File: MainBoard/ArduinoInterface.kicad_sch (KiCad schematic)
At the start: 22 parts, among them J2 SDCard Header, U1 74HC165, U1 IDT7024L15PFG, U10 74HC595, U2 74HC165, U2 ATF22V10C, U4 74HC595, U5 74AHCT04, U7 74HC595, U8 74HC595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

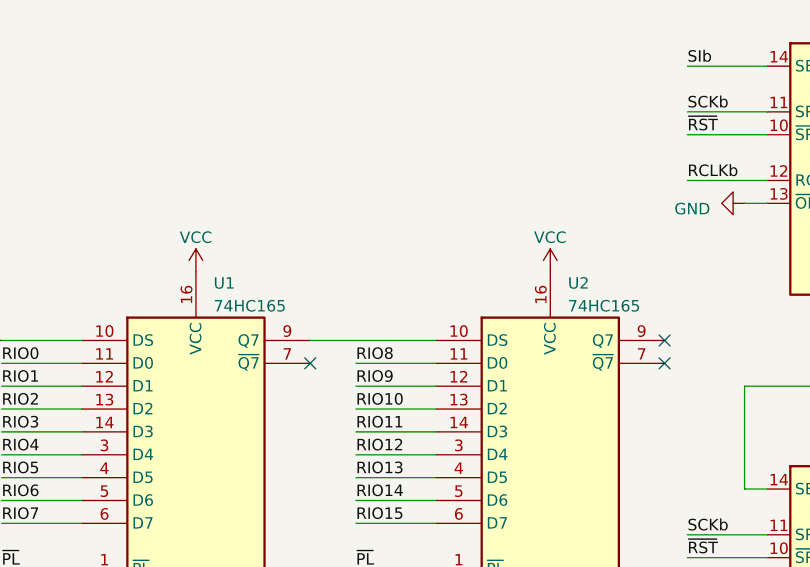
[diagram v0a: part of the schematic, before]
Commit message: MainBoard: Update BOM, PCB printout, and Gerber plots
This includes changes to add the Arduino interface to the main board PCB.
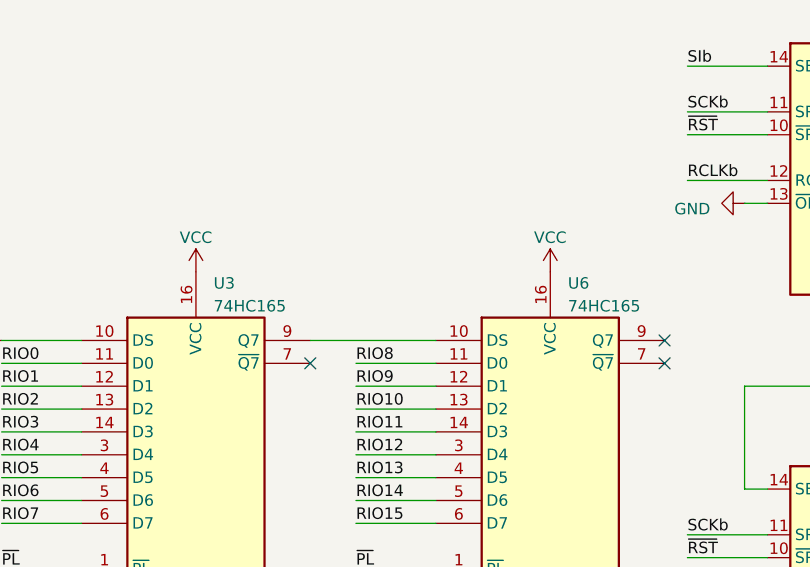
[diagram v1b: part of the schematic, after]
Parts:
- renumbered U1 to U3, U2 to U6
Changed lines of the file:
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@@
   (symbol (lib_id "74xx:74HC165") (at 162.56 71.12 0) (unit 1)
     (in_bom yes) (on_board yes) (dnp no) (fields_autoplaced)
-    (property "Reference" "U2" (at 164.5159 49.53 0)
+    (property "Reference" "U6" (at 164.5159 49.53 0)
       (effects (font (size 1.27 1.27)) (justify left))
     )
@@
   (symbol (lib_id "74xx:74HC165") (at 123.19 71.12 0) (unit 1)
     (in_bom yes) (on_board yes) (dnp no) (fields_autoplaced)
-    (property "Reference" "U1" (at 125.1459 49.53 0)
+    (property "Reference" "U3" (at 125.1459 49.53 0)
       (effects (font (size 1.27 1.27)) (justify left))
     )
@@
   (symbol (lib_id "power:GND") (at 162.56 96.52 0) (unit 1)
     (in_bom yes) (on_board yes) (dnp no) (fields_autoplaced)
-    (property "Reference" "#PWR026" (at 162.56 102.87 0)
+    (property "Reference" "#PWR029" (at 162.56 102.87 0)
       (effects (font (size 1.27 1.27)) hide)
     )
@@
   (symbol (lib_id "power:VCC") (at 162.56 48.26 0) (unit 1)
     (in_bom yes) (on_board yes) (dnp no) (fields_autoplaced)
-    (property "Reference" "#PWR025" (at 162.56 52.07 0)
-      (effects (font (size 1.27 1.27)) hide)
-    )
+    (property "Reference" "#PWR028" (at 162.56 52.07 0)
+      (effects (font (size 1.27 1.27)) hide)
+    )

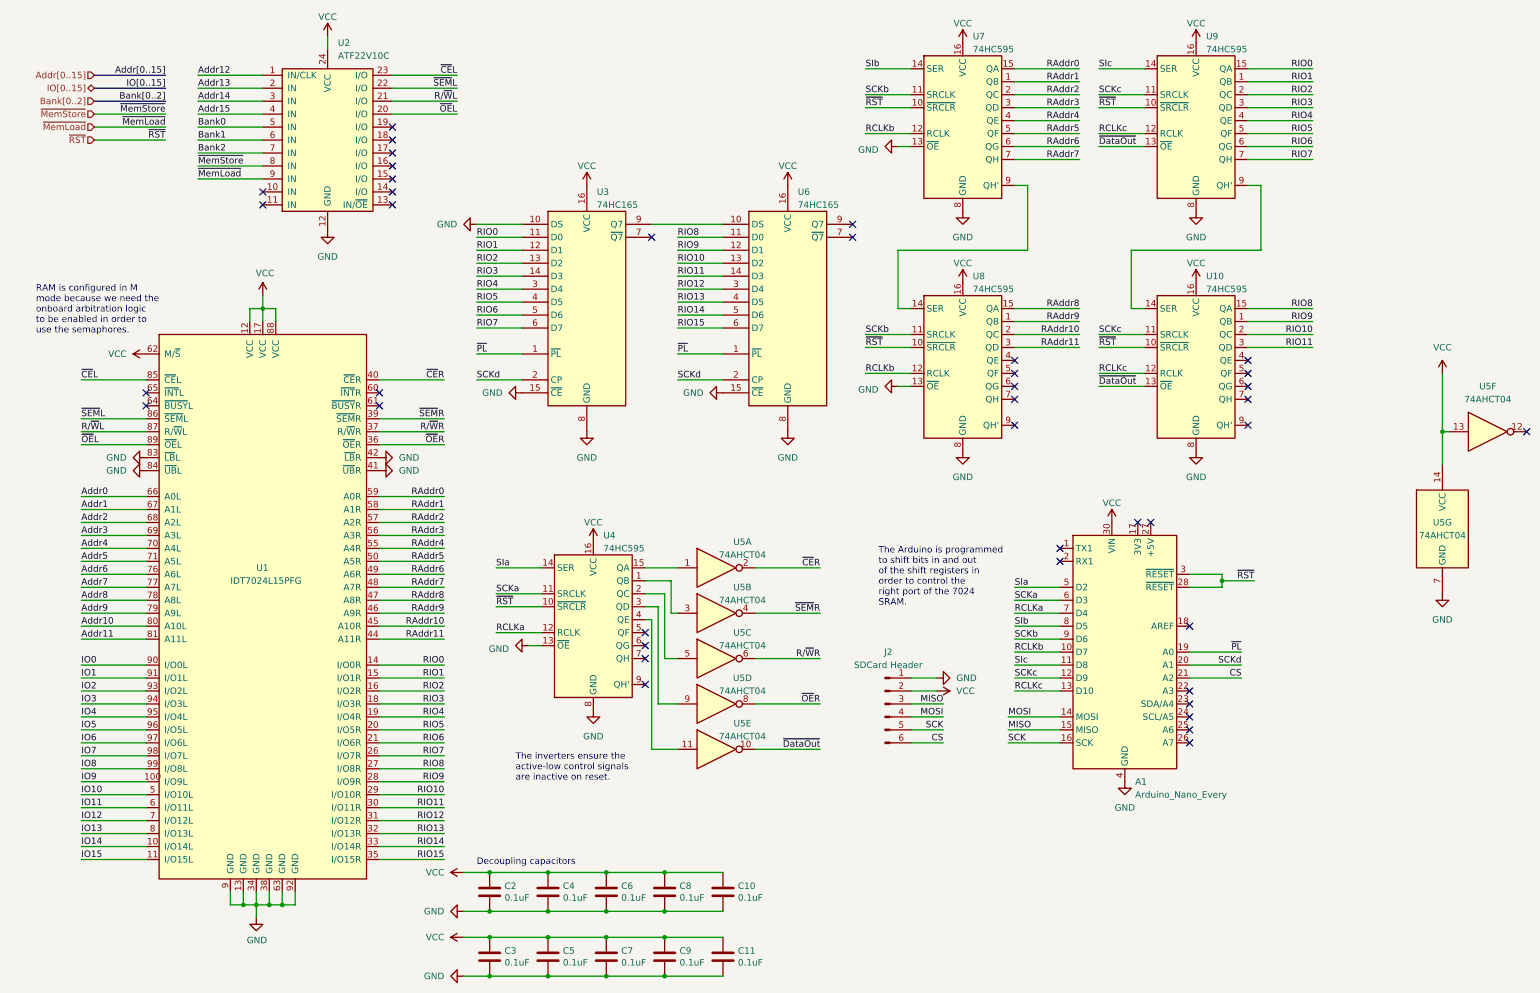
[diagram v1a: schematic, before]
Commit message: MainBoard: Use footprints symbols from the Turtle16 library
These symbols will be consistent across the Turtle16 project and will each
contain manufacturer, mfr. #, Mouser #, and Digikey #.
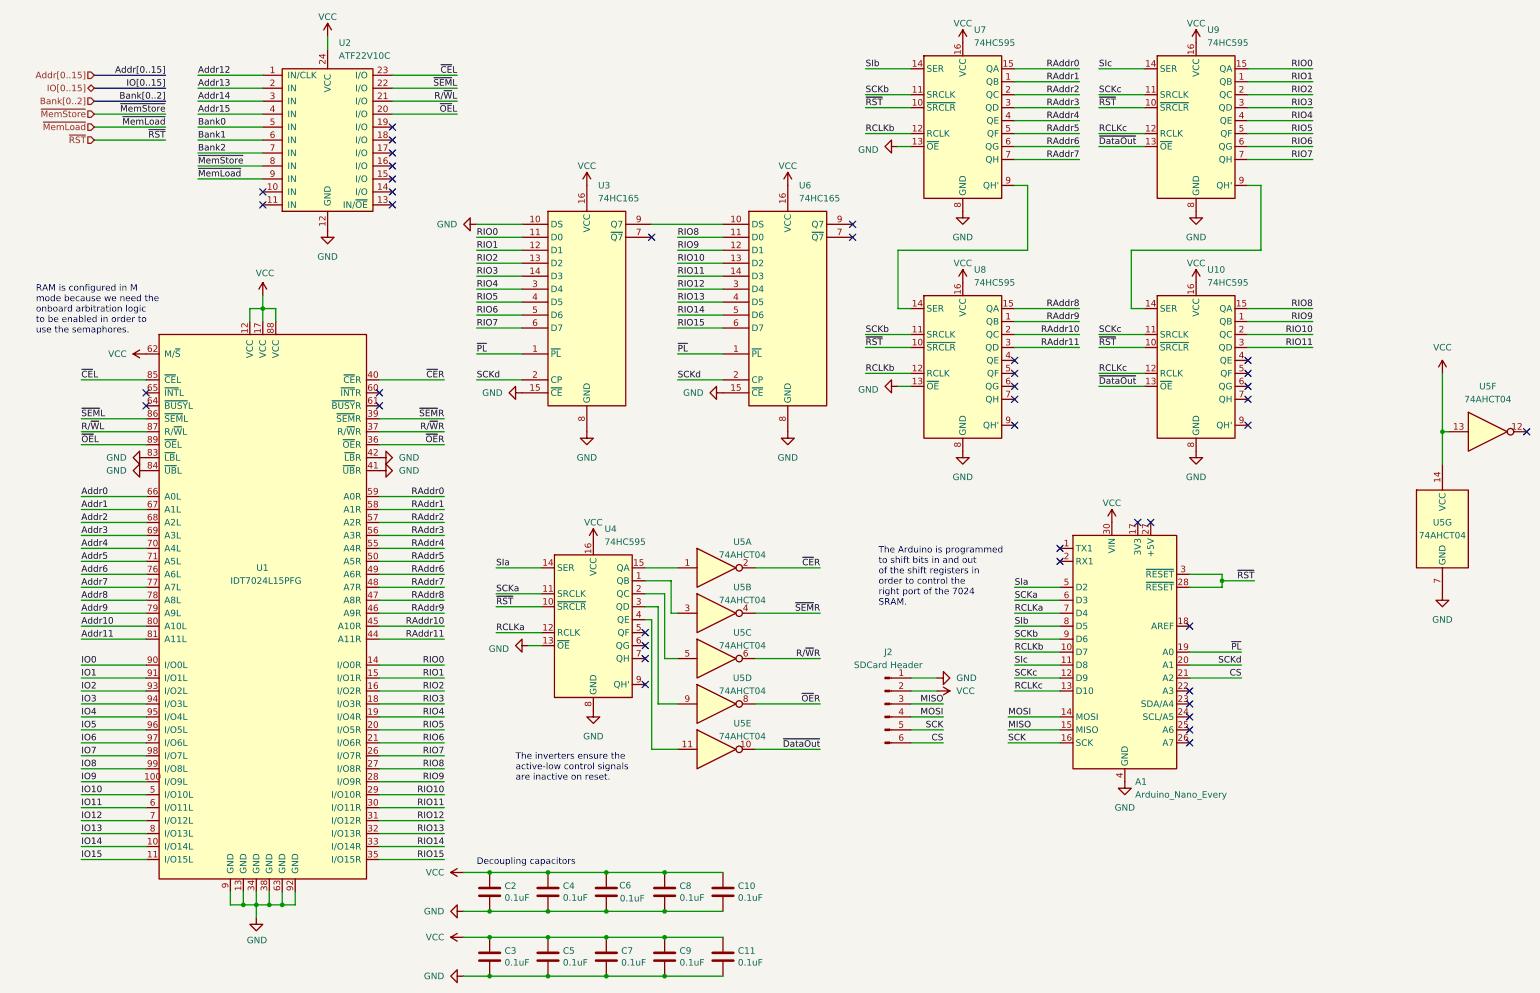
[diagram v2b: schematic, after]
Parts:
- C10, C11, C2, C3, C4, C5, C6, C7, C8, C9: footprint Capacitor_SMD:C_0603_1608Metric_Pad1.08x0.95mm_HandSolder -> Capacitor_SMD:C_0603_1608Metric; Digikey# (none) -> 587-6004-1-ND; Manufacturer (none) -> Taiyo Yuden; Manufacturer# (none) -> EMK107B7104KAHT; Mouser https://www.mouser.com/ProductDetail/963-EMK107B7104KAHT -> (none); Mouser# (none) -> 963-EMK107B7104KAHT
- U1: symbol MainBoard-rescue:IDT7024L15PFG-Memory_RAM -> Turtle16:IDT7024L15PFG; Digikey# (none) -> 800-3611-ND; Manufacturer (none) -> Renesas Electronics Corporation; Manufacturer# (none) -> 7024L15PFG; Mouser https://www.mouser.com/ProductDetail/Renesas-IDT/7024L15PFG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 -> (none); Mouser# (none) -> 972-7024L15PFG
- U10, U4, U7, U8, U9: symbol 74xx:74HC595 -> Turtle16:74HC595; Digikey# (none) -> 1727-1012-1-ND; Manufacturer (none) -> Nexperia; Manufacturer# (none) -> 74HC595PW-Q100,118; Mouser# (none) -> 771-74HC595PW-Q100
- U2: symbol MEMModule-rescue:ATF22V10C-Logic_Programmable -> Turtle16:ATF22V10C; Digikey# (none) -> ATF22V10C-7PX-ND; Manufacturer (none) -> Microchip Technology; Manufacturer# (none) -> ATF22V10C-7PX; Mouser# (none) -> 556-AF22V10C7PX
- U3, U6: symbol 74xx:74HC165 -> Turtle16:74HC165; Digikey# (none) -> 1727-8390-1-ND; Manufacturer (none) -> Nexperia; Manufacturer# (none) -> 74HC165PW-Q100,118; Mouser# (none) -> 771-74HC165PWQ100118
- U5: symbol 74xx:74AHCT04 -> Turtle16:74AHCT04; Digikey# (none) -> 1727-74AHCT04APWJCT-ND; Manufacturer (none) -> Nexperia; Manufacturer# (none) -> 74AHCT04APWJ; Mouser# (none) -> 771-74AHCT04APWJ

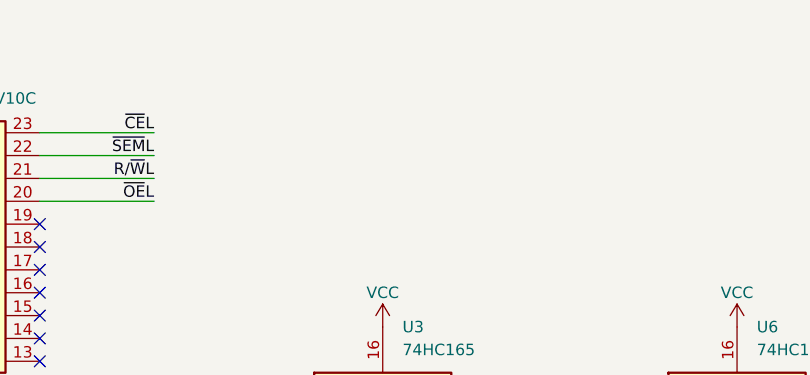
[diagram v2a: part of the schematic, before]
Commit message: MainBoard: Move all components to the top side
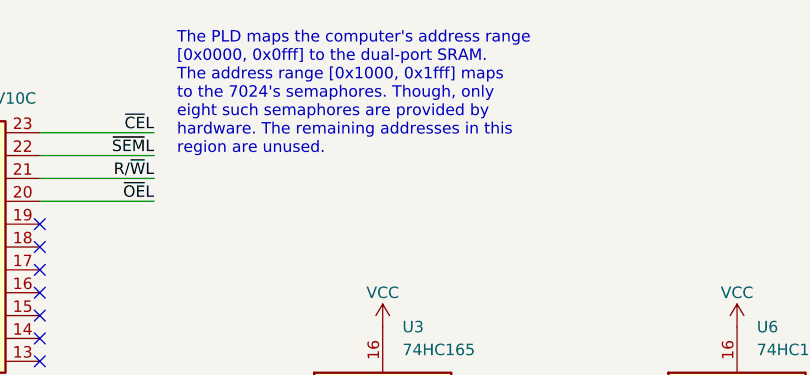
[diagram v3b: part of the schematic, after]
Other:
- note added: "The PLD maps the computer's address range [0x0000, 0x0fff] to the dual-port SRAM. The address range [0x1000, 0x1fff] maps to the 7024's semaphores. Though, only eight such semaphores are provided by hardware. The remaining addresses in this region are unused."
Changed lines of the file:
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@@
+    (effects (font (size 1.27 1.27)) (justify left bottom))
+  )
+  (text "The PLD maps the computer's address range\n[0x0000, 0x0fff] to the dual-port SRAM.\nThe address range [0x1000, 0x1fff] maps\nto the 7024's semaphores. Though, only\neight such semaphores are provided by\nhardware. The remaining addresses in this\nregion are unused."
+    (at 100.33 29.21 0)
     (effects (font (size 1.27 1.27)) (justify left bottom))
   )

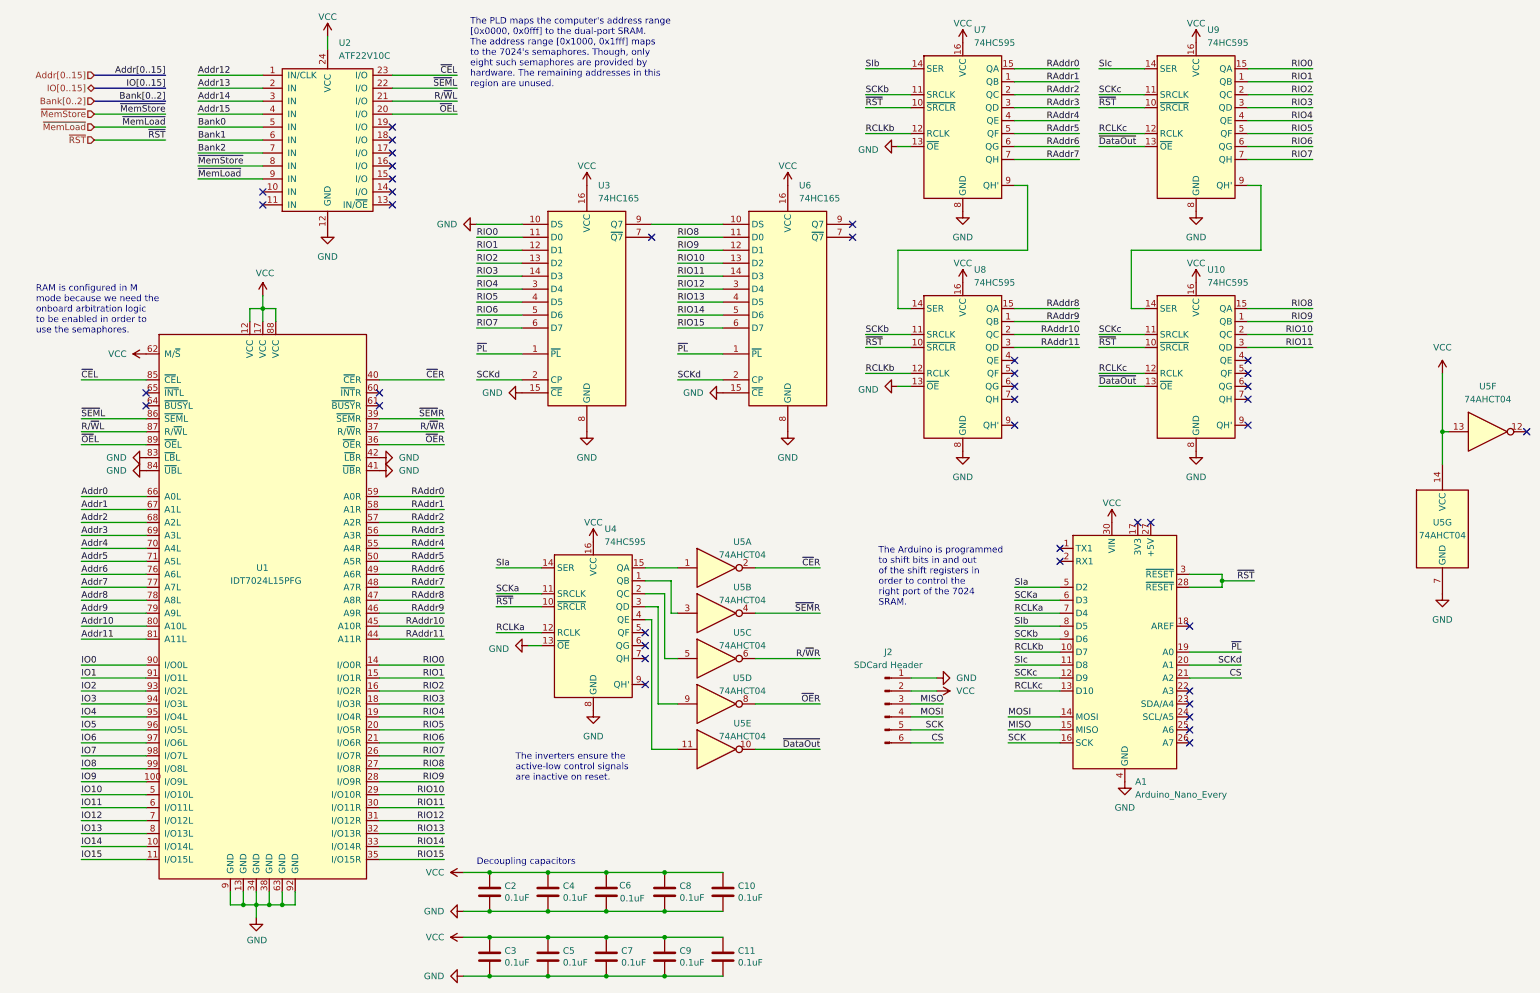
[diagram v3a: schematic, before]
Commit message: MainBoard: Break schematic up into hierarchical sheets for increased readability
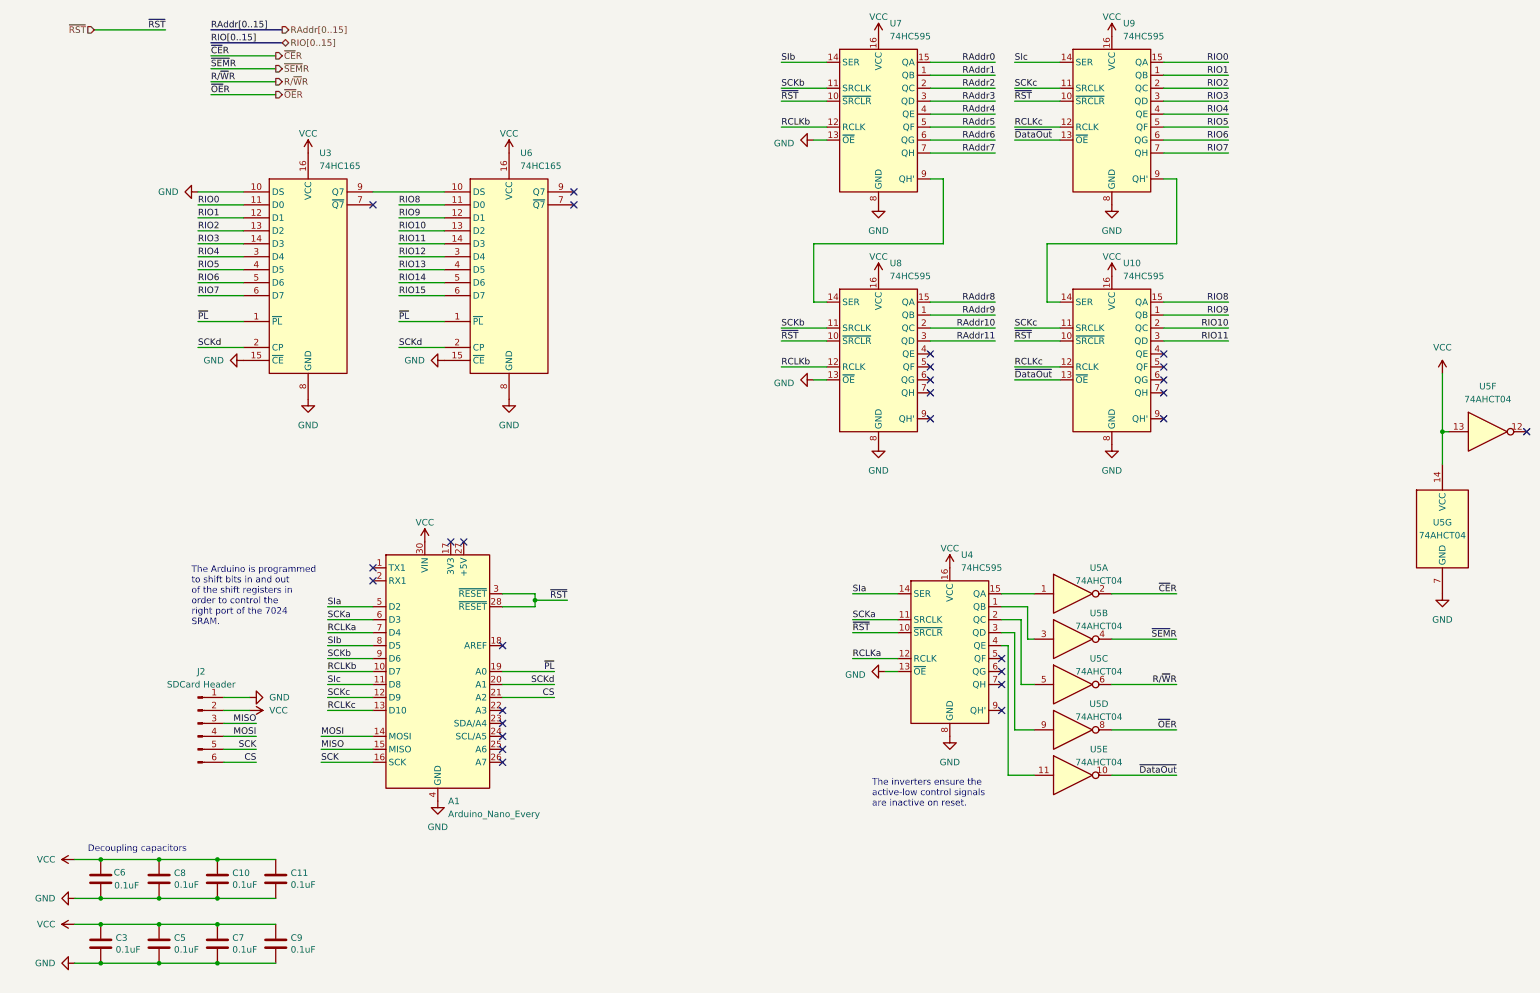
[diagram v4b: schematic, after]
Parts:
- removed C2, C4: 0.1uF, Capacitor_SMD:C_0603_1608Metric, symbol Device:C
- removed U1: IDT7024L15PFG, Package_QFP:TQFP-100_14x14mm_P0.5mm, symbol Turtle16:IDT7024L15PFG
- removed U2: ATF22V10C, Package_DIP:DIP-24_W7.62mm_Socket, symbol Turtle16:ATF22V10C
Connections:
- no-connect marks 41 -> 28
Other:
- note removed: "RAM is configured in M mode because we need the onboard arbitration logic to be enabled in order to use the semaphores."
- note removed: "The PLD maps the computer's address range [0x0000, 0x0fff] to the dual-port SRAM. The address range [0x1000, 0x1fff] maps to the 7024's semaphores. Though, only eight such semaphores are provided by hardware. The remaining addresses in this region are unused."
- moved on the sheet: A1, C10, C11, C3, C5, C6, C7, C8, C9, J2, U10, U3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
